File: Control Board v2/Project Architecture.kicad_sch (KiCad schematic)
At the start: 0 parts

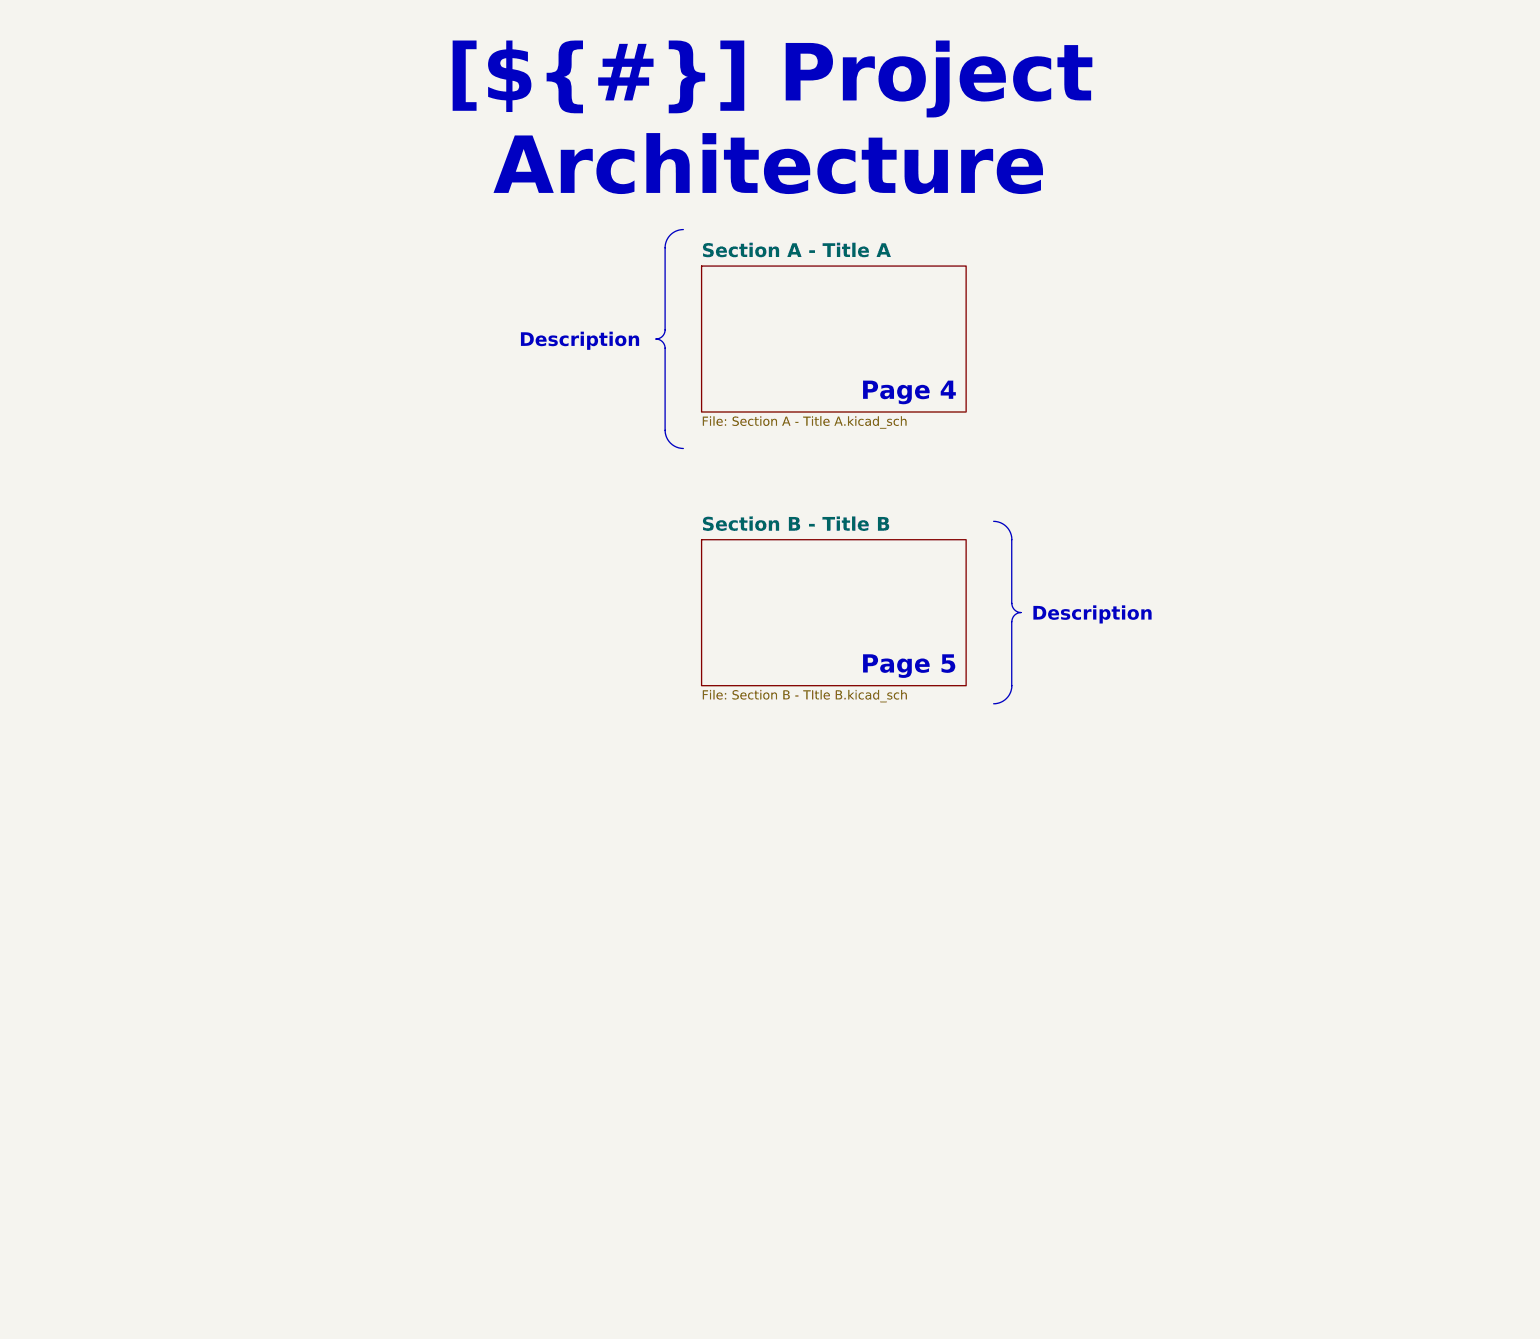
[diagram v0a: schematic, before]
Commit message: Finish preparing the template for v2 design
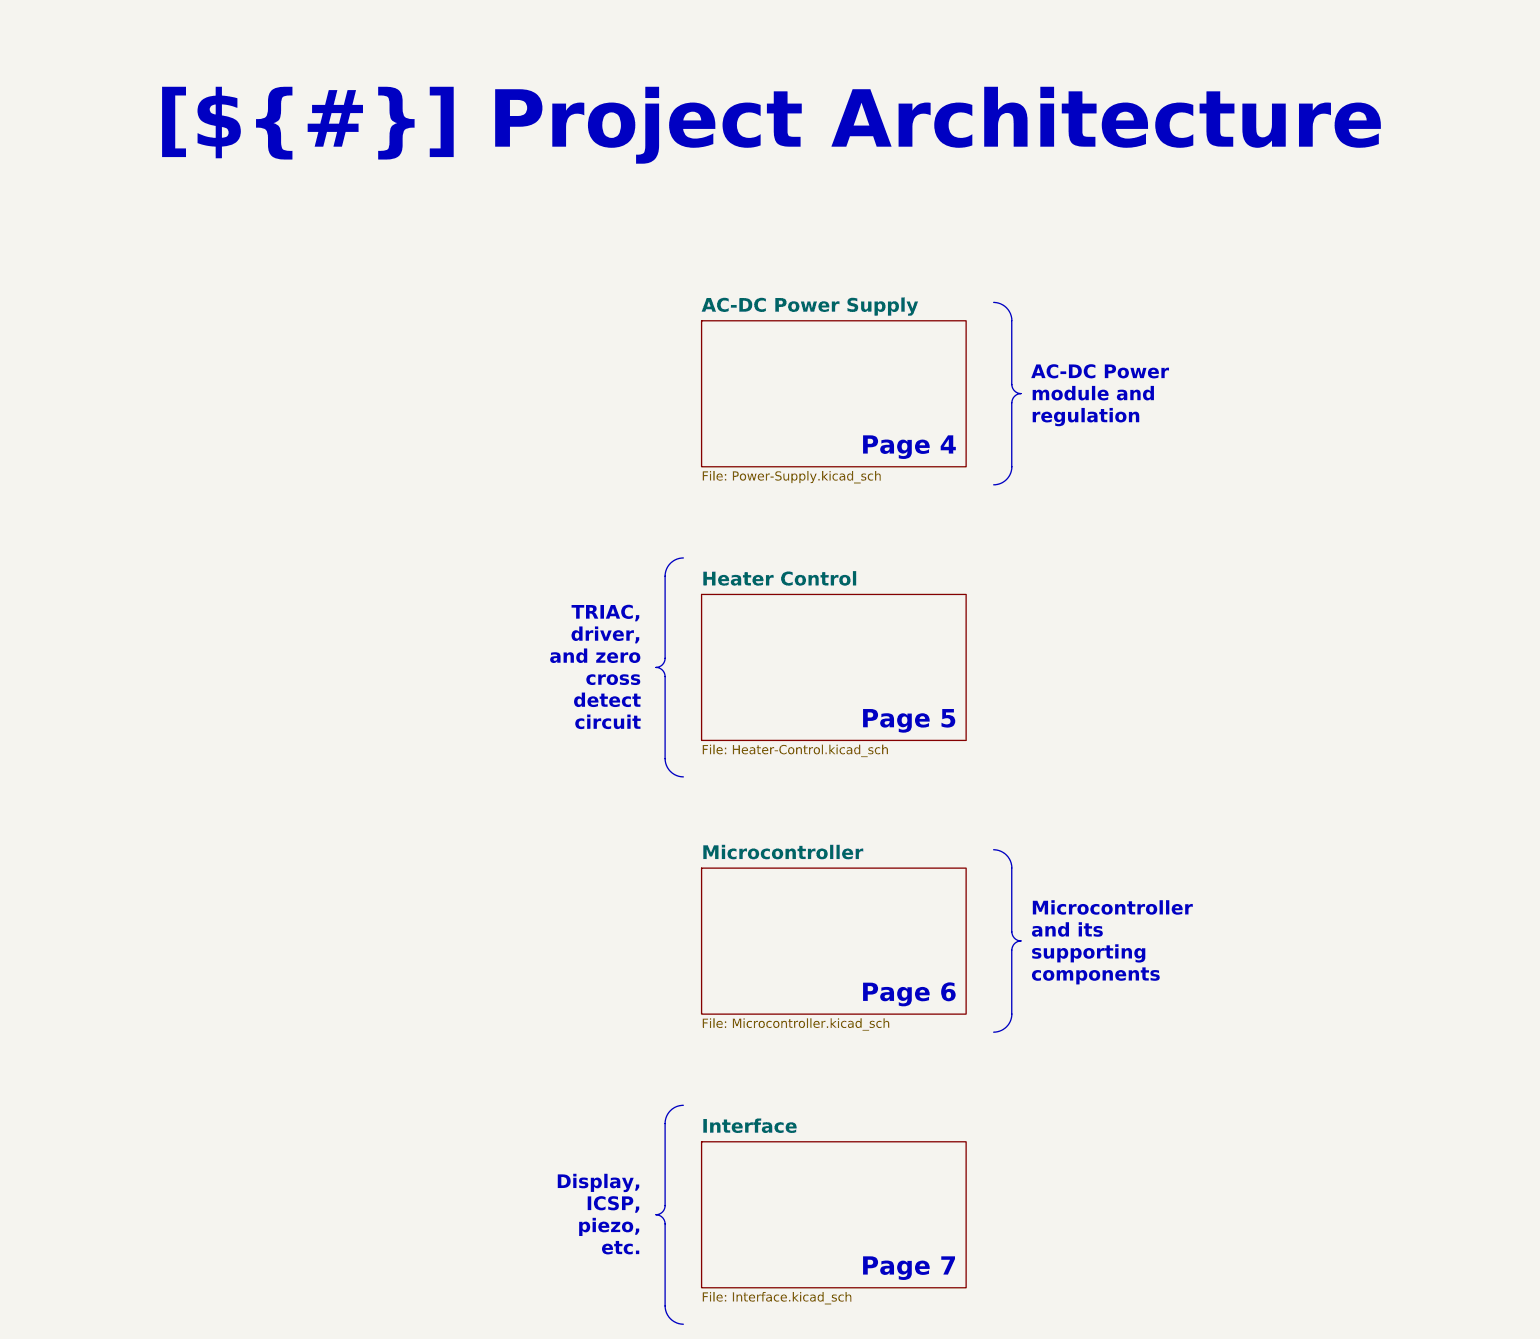
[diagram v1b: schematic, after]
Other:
- sheet Section A - Title A renamed Microcontroller
- sheet Section B - Title B renamed Interface
- added sheet AC-DC Power Supply (Power-Supply.kicad_sch)
- added sheet Heater Control (Heater-Control.kicad_sch)
- sheet Interface: file Section B - TItle B.kicad_sch -> Interface.kicad_sch
- sheet Microcontroller: file Section A - Title A.kicad_sch -> Microcontroller.kicad_sch
- note added: "Page 6"
- note added: "Page 7"
